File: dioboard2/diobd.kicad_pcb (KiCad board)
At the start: 2 copper layers, 58.4 x 15.2 mm, 9 parts, among them J1 Conn_01x03, J2 Conn_01x03, J3 Conn_01x03, J4 Conn_01x03

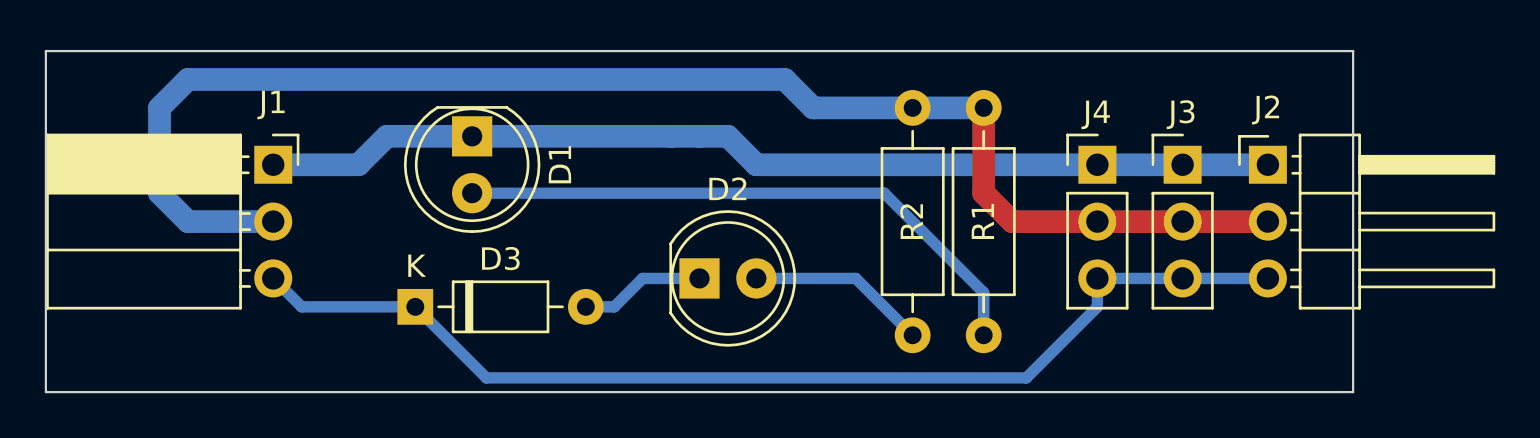
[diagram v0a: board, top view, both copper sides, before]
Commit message: delete traces and shrink board outline by moving parts
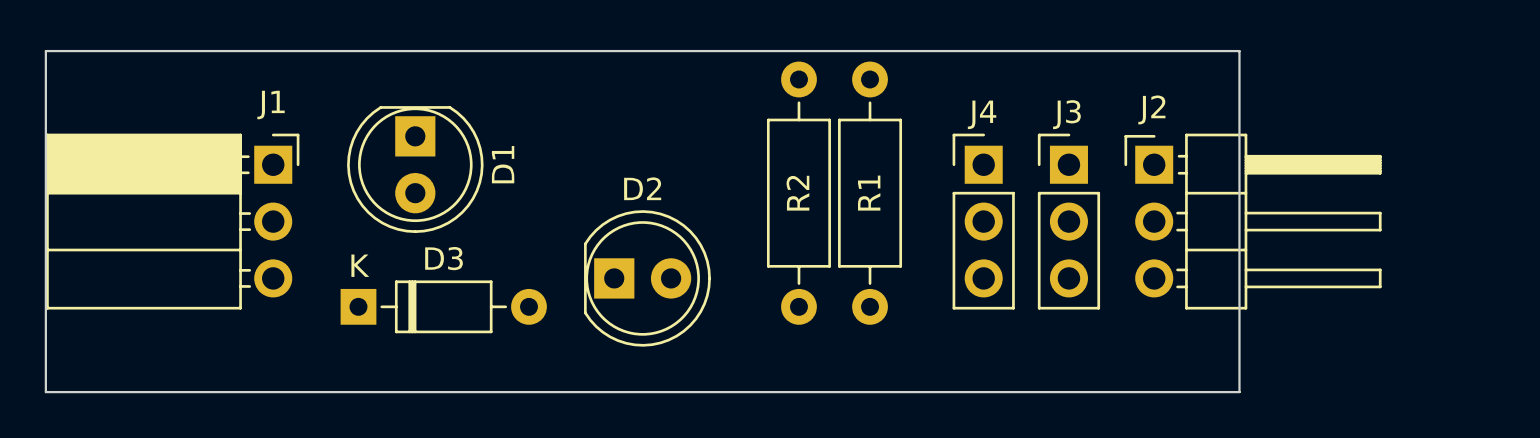
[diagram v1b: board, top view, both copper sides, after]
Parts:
- moved R2 5.24 mm to (127.6, 88.9)
- moved R1 5.24 mm to (130.8, 88.9)
- moved J2 5.08 mm to (143.5, 92.7)
- moved J3 5.08 mm to (139.7, 92.7)
- moved J4 5.08 mm to (135.9, 92.7)
- moved D2 3.81 mm to (119.4, 97.8)
- moved D1 2.54 mm to (110.5, 91.4)
- moved D3 2.54 mm to (108.0, 99.1)
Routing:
- net +5V: track 64.3 -> 0.00 mm
- net /signal: track 48.9 -> 0.00 mm
- net Earth: track 45.5 -> 0.00 mm
- net Net-(D1-Pad2): track 26.6 -> 0.00 mm
- net Net-(D2-Pad2): track 8.04 -> 0.00 mm
- net Net-(D2-Pad1): track 5.61 -> 0.00 mm
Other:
- board size 58.4 x 15.2 mm -> 53.3 x 15.2 mm
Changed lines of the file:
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@@
-(kicad_pcb (version 20171130) (host pcbnew 5.0.0)
+(kicad_pcb (version 20171130) (host pcbnew "(5.0.1)-3")
   (general
     (thickness 1.5748)
     (drawings 4)
-    (tracks 33)
+    (tracks 0)
     (zones 0)
     (modules 9)
@@
   )
   (setup
-    (last_trace_width 0.508)
+    (last_trace_width 0.2032)
     (user_trace_width 0.254)
     (user_trace_width 0.508)
@@
     (pad_drill 0.6)
     (pad_to_mask_clearance 0)
+    (solder_mask_min_width 0.25)
     (aux_axis_origin 0 0)
     (grid_origin 93.98 102.87)
-    (visible_elements FFFFFF7F)
+    (visible_elements 7FFFFFFF)
     (pcbplotparams
       (layerselection 0x010fc_ffffffff)
@@
   )
   (module LED_THT:LED_D5.0mm (layer F.Cu)
-    (at 113.03 91.44 270)
+    (at 110.49 91.44 270)
     (descr "LED, diameter 5.0mm, 2 pins, http://cdn-reichelt.de/documents/datenblatt/A500/LL-504BC2E-009.pdf")
     (tags "LED diameter 5.0mm 2 pins")
@@
   )
   (module LED_THT:LED_D5.0mm (layer F.Cu)
-    (at 123.19 97.79)
+    (at 119.38 97.79)
     (descr "LED, diameter 5.0mm, 2 pins, http://cdn-reichelt.de/documents/datenblatt/A500/LL-504BC2E-009.pdf")
     (tags "LED diameter 5.0mm 2 pins")
@@
   )
   (module Diode_THT:D_DO-35_SOD27_P7.62mm_Horizontal (layer F.Cu)
-    (at 110.49 99.06)
+    (at 107.95 99.06)
     (descr "Diode, DO-35_SOD27 series, Axial, Horizontal, pin pitch=7.62mm, , length*diameter=4*2mm^2, , http://www.diodes.com/_files/packages/DO-35.pdf")
     (tags "Diode DO-35_SOD27 series Axial Horizontal pin pitch 7.62mm  length 4mm diameter 2mm")
@@
   )
   (module Connector_PinHeader_2.54mm:PinHeader_1x03_P2.54mm_Horizontal (layer F.Cu)
-    (at 148.59 92.71)
+    (at 143.51 92.71)
     (descr "Through hole angled pin header, 1x03, 2.54mm pitch, 6mm pin length, single row")
     (tags "Through hole angled pin header THT 1x03 2.54mm single row")
@@
   )
   (module Connector_PinHeader_2.54mm:PinHeader_1x03_P2.54mm_Vertical (layer F.Cu)
-    (at 144.78 92.71)
+    (at 139.7 92.71)
     (descr "Through hole straight pin header, 1x03, 2.54mm pitch, single row")
     (tags "Through hole pin header THT 1x03 2.54mm single row")
@@
   )
   (module Connector_PinHeader_2.54mm:PinHeader_1x03_P2.54mm_Vertical (layer F.Cu)
-    (at 140.97 92.71)
+    (at 135.89 92.71)
     (descr "Through hole straight pin header, 1x03, 2.54mm pitch, single row")
     (tags "Through hole pin header THT 1x03 2.54mm single row")
@@
   )
   (module Resistor_THT:R_Axial_DIN0207_L6.3mm_D2.5mm_P10.16mm_Horizontal (layer F.Cu)
-    (at 135.89 90.17 270)
+    (at 130.81 88.9 270)
     (descr "Resistor, Axial_DIN0207 series, Axial, Horizontal, pin pitch=10.16mm, 0.25W = 1/4W, length*diameter=6.3*2.5mm^2, http://cdn-reichelt.de/documents/datenblatt/B400/1_4W%23YAG.pdf")
     (tags "Resistor Axial_DIN0207 series Axial Horizontal pin pitch 10.16mm 0.25W = 1/4W length 6.3mm diameter 2.5mm")
@@
   )
   (module Resistor_THT:R_Axial_DIN0207_L6.3mm_D2.5mm_P10.16mm_Horizontal (layer F.Cu)
-    (at 132.715 90.17 270)
+    (at 127.635 88.9 270)
     (descr "Resistor, Axial_DIN0207 series, Axial, Horizontal, pin pitch=10.16mm, 0.25W = 1/4W, length*diameter=6.3*2.5mm^2, http://cdn-reichelt.de/documents/datenblatt/B400/1_4W%23YAG.pdf")
     (tags "Resistor Axial_DIN0207 series Axial Horizontal pin pitch 10.16mm 0.25W = 1/4W length 6.3mm diameter 2.5mm")
@@
   )
   (gr_line (start 93.98 87.63) (end 93.98 102.87) (layer Edge.Cuts) (width 0.1))
-  (gr_line (start 152.4 87.63) (end 93.98 87.63) (layer Edge.Cuts) (width 0.1))
-  (gr_line (start 152.4 102.87) (end 152.4 87.63) (layer Edge.Cuts) (width 0.1))
-  (gr_line (start 93.98 102.87) (end 152.4 102.87) (layer Edge.Cuts) (width 0.1))
-  (segment (start 135.89 100.33) (end 135.89 98.425) (width 0.508) (layer B.Cu) (net 1))
-  (segment (start 131.445 93.98) (end 113.03 93.98) (width 0.508) (layer B.Cu) (net 1))
-  (segment (start 135.89 98.425) (end 131.445 93.98) (width 0.508) (layer B.Cu) (net 1))
-  (segment (start 104.14 92.71) (end 107.95 92.71) (width 1.016) (layer B.Cu) (net 2))
-  (segment (start 109.22 91.44) (end 113.03 91.44) (width 1.016) (layer B.Cu) (net 2))
-  (segment (start 107.95 92.71) (end 109.22 91.44) (width 1.016) (layer B.Cu) (net 2))
-  (segment (start 125.73 92.71) (end 148.59 92.71) (width 1.016) (layer B.Cu) (net 2))
-  (segment (start 113.03 91.44) (end 121.92 91.44) (width 1.016) (layer B.Cu) (net 2))
-  (segment (start 121.92 91.44) (end 123.19 91.44) (width 1.016) (layer B.Cu) (net 2))
-  (segment (start 123.19 91.44) (end 124.46 91.44) (width 1.016) (layer B.Cu) (net 2))
-  (segment (start 124.46 91.44) (end 125.73 92.71) (width 1.016) (layer B.Cu) (net 2))
-  (segment (start 118.11 99.06) (end 119.38 99.06) (width 0.508) (layer B.Cu) (net 3))
-  (segment (start 120.65 97.79) (end 123.19 97.79) (width 0.508) (layer B.Cu) (net 3))
-  (segment (start 119.38 99.06) (end 120.65 97.79) (width 0.508) (layer B.Cu) (net 3))
-  (segment (start 130.175 97.79) (end 132.715 100.33) (width 0.508) (layer B.Cu) (net 4))
-  (segment (start 125.73 97.79) (end 130.175 97.79) (width 0.508) (layer B.Cu) (net 4))
-  (segment (start 148.59 97.79) (end 140.97 97.79) (width 0.508) (layer B.Cu) (net 5))
-  (segment (start 113.665 102.235) (end 110.49 99.06) (width 0.508) (layer B.Cu) (net 5))
-  (segment (start 137.795 102.235) (end 113.665 102.235) (width 0.508) (layer B.Cu) (net 5))
-  (segment (start 140.97 99.06) (end 137.795 102.235) (width 0.508) (layer B.Cu) (net 5))
-  (segment (start 140.97 97.79) (end 140.97 99.06) (width 0.508) (layer B.Cu) (net 5))
-  (segment (start 105.41 99.06) (end 104.14 97.79) (width 0.508) (layer B.Cu) (net 5))
-  (segment (start 110.49 99.06) (end 105.41 99.06) (width 0.508) (layer B.Cu) (net 5))
-  (segment (start 128.27 90.17) (end 135.89 90.17) (width 1.016) (layer B.Cu) (net 6))
-  (segment (start 127 88.9) (end 128.27 90.17) (width 1.016) (layer B.Cu) (net 6))
-  (segment (start 100.33 88.9) (end 127 88.9) (width 1.016) (layer B.Cu) (net 6))
-  (segment (start 104.14 95.25) (end 100.33 95.25) (width 1.016) (layer B.Cu) (net 6))
-  (segment (start 99.06 93.98) (end 99.06 90.17) (width 1.016) (layer B.Cu) (net 6))
-  (segment (start 100.33 95.25) (end 99.06 93.98) (width 1.016) (layer B.Cu) (net 6))
-  (segment (start 99.06 90.17) (end 100.33 88.9) (width 1.016) (layer B.Cu) (net 6))
-  (segment (start 137.16 95.25) (end 135.89 93.98) (width 1.016) (layer F.Cu) (net 6))
-  (segment (start 135.89 93.98) (end 135.89 90.17) (width 1.016) (layer F.Cu) (net 6))
-  (segment (start 148.59 95.25) (end 137.16 95.25) (width 1.016) (layer F.Cu) (net 6))
+  (gr_line (start 147.32 87.63) (end 93.98 87.63) (layer Edge.Cuts) (width 0.1))
+  (gr_line (start 147.32 102.87) (end 147.32 87.63) (layer Edge.Cuts) (width 0.1))
+  (gr_line (start 93.98 102.87) (end 147.32 102.87) (layer Edge.Cuts) (width 0.1))
 )

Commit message: Finished preliminary routing
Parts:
- moved R1 1.27 mm to (130.8, 90.2)
- moved R2 1.27 mm to (127.6, 90.2)
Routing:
- net +5V: track 0.00 -> 45.8 mm
- net Net-(D1-Pad2): track 0.00 -> 44.8 mm
- net Earth: track 0.00 -> 44.0 mm
- net /signal: track 0.00 -> 42.5 mm
- net Net-(D2-Pad2): track 0.00 -> 6.77 mm
- net Net-(D2-Pad1): track 0.00 -> 4.34 mm
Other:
- net class Default: clearance 0.2032 -> 0.254; trace_width 0.2032 -> 0.254
- rule trace_clearance: 0.2032 -> 0.254
- rule trace_min: 0.2032 -> 0.254
- rule via_min_drill: 0.254 -> 0.381
- rule via_min_size: 0.635 -> 0.7874
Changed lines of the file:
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@@
     (thickness 1.5748)
     (drawings 4)
-    (tracks 0)
+    (tracks 40)
     (zones 0)
     (modules 9)
@@
   )
   (setup
-    (last_trace_width 0.2032)
+    (last_trace_width 0.254)
     (user_trace_width 0.254)
     (user_trace_width 0.508)
@@
     (user_trace_width 1.016)
     (user_trace_width 1.27)
-    (trace_clearance 0.2032)
+    (trace_clearance 0.254)
     (zone_clearance 0.508)
     (zone_45_only no)
-    (trace_min 0.2032)
+    (trace_min 0.254)
     (segment_width 0.2)
     (edge_width 0.1)
     (via_size 0.7874)
     (via_drill 0.381)
-    (via_min_size 0.635)
-    (via_min_drill 0.254)
+    (via_min_size 0.7874)
+    (via_min_drill 0.381)
     (uvia_size 0.7874)
     (uvia_drill 0.381)
@@
   (net 6 +5V)
   (net_class Default "This is the default net class."
-    (clearance 0.2032)
-    (trace_width 0.2032)
+    (clearance 0.254)
+    (trace_width 0.254)
     (via_dia 0.7874)
     (via_drill 0.381)
@@
     (uvia_drill 0.381)
     (diff_pair_gap 0.2032)
-    (diff_pair_width 0.2032)
+    (diff_pair_width 0.254)
     (add_net +5V)
     (add_net /signal)
@@
   )
   (module Resistor_THT:R_Axial_DIN0207_L6.3mm_D2.5mm_P10.16mm_Horizontal (layer F.Cu)
-    (at 130.81 88.9 270)
+    (at 130.81 90.17 270)
     (descr "Resistor, Axial_DIN0207 series, Axial, Horizontal, pin pitch=10.16mm, 0.25W = 1/4W, length*diameter=6.3*2.5mm^2, http://cdn-reichelt.de/documents/datenblatt/B400/1_4W%23YAG.pdf")
     (tags "Resistor Axial_DIN0207 series Axial Horizontal pin pitch 10.16mm 0.25W = 1/4W length 6.3mm diameter 2.5mm")
@@
   )
   (module Resistor_THT:R_Axial_DIN0207_L6.3mm_D2.5mm_P10.16mm_Horizontal (layer F.Cu)
-    (at 127.635 88.9 270)
+    (at 127.635 90.17 270)
     (descr "Resistor, Axial_DIN0207 series, Axial, Horizontal, pin pitch=10.16mm, 0.25W = 1/4W, length*diameter=6.3*2.5mm^2, http://cdn-reichelt.de/documents/datenblatt/B400/1_4W%23YAG.pdf")
     (tags "Resistor Axial_DIN0207 series Axial Horizontal pin pitch 10.16mm 0.25W = 1/4W length 6.3mm diameter 2.5mm")
@@
   (gr_line (start 147.32 102.87) (end 147.32 87.63) (layer Edge.Cuts) (width 0.1))
   (gr_line (start 93.98 102.87) (end 147.32 102.87) (layer Edge.Cuts) (width 0.1))
+  (segment (start 102.87 93.98) (end 101.6 95.25) (width 0.254) (layer B.Cu) (net 1))
+  (segment (start 110.49 93.98) (end 102.87 93.98) (width 0.254) (layer B.Cu) (net 1))
+  (segment (start 101.6 95.25) (end 101.6 99.06) (width 0.254) (layer B.Cu) (net 1))
+  (segment (start 130.010001 101.129999) (end 130.81 100.33) (width 0.254) (layer B.Cu) (net 1))
+  (segment (start 101.6 99.06) (end 105.02979 102.48979) (width 0.254) (layer B.Cu) (net 1))
+  (segment (start 105.02979 102.48979) (end 128.65021 102.48979) (width 0.254) (layer B.Cu) (net 1))
+  (segment (start 128.65021 102.48979) (end 130.010001 101.129999) (width 0.254) (layer B.Cu) (net 1))
+  (segment (start 143.51 92.71) (end 135.89 92.71) (width 1.016) (layer B.Cu) (net 2))
+  (segment (start 112.406 91.44) (end 110.49 91.44) (width 1.016) (layer B.Cu) (net 2))
+  (segment (start 115.45479 88.39121) (end 112.406 91.44) (width 1.016) (layer B.Cu) (net 2))
+  (segment (start 133.43721 88.39121) (end 115.45479 88.39121) (width 1.016) (layer B.Cu) (net 2))
+  (segment (start 135.89 90.844) (end 133.43721 88.39121) (width 1.016) (layer B.Cu) (net 2))
+  (segment (start 135.89 92.71) (end 135.89 90.844) (width 1.016) (layer B.Cu) (net 2))
+  (segment (start 104.14 92.71) (end 106.68 92.71) (width 1.016) (layer B.Cu) (net 2))
+  (segment (start 107.95 91.44) (end 110.49 91.44) (width 1.016) (layer B.Cu) (net 2))
+  (segment (start 106.68 92.71) (end 107.95 91.44) (width 1.016) (layer B.Cu) (net 2))
+  (segment (start 115.57 99.06) (end 118.11 99.06) (width 0.254) (layer B.Cu) (net 3))
+  (segment (start 118.11 99.06) (end 119.38 97.79) (width 0.254) (layer B.Cu) (net 3))
+  (segment (start 121.92 97.79) (end 124.46 100.33) (width 0.254) (layer B.Cu) (net 4))
+  (segment (start 124.46 100.33) (end 127.635 100.33) (width 0.254) (layer B.Cu) (net 4))
+  (segment (start 135.89 97.79) (end 143.51 97.79) (width 0.254) (layer B.Cu) (net 5))
+  (segment (start 125.741592 97.79) (end 123.201592 95.25) (width 0.254) (layer B.Cu) (net 5))
+  (segment (start 135.89 97.79) (end 125.741592 97.79) (width 0.254) (layer B.Cu) (net 5))
+  (segment (start 109.004 99.06) (end 110.274 97.79) (width 0.254) (layer B.Cu) (net 5))
+  (segment (start 107.95 99.06) (end 109.004 99.06) (width 0.254) (layer B.Cu) (net 5))
+  (segment (start 110.274 97.79) (end 115.57 97.79) (width 0.254) (layer B.Cu) (net 5))
+  (segment (start 115.57 97.79) (end 118.11 95.25) (width 0.254) (layer B.Cu) (net 5))
+  (segment (start 118.11 95.25) (end 123.201592 95.25) (width 0.254) (layer B.Cu) (net 5))
+  (segment (start 104.14 97.79) (end 105.41 99.06) (width 0.254) (layer B.Cu) (net 5))
+  (segment (start 105.41 99.06) (end 107.95 99.06) (width 0.254) (layer B.Cu) (net 5))
+  (segment (start 143.51 95.25) (end 135.89 95.25) (width 1.016) (layer B.Cu) (net 6))
+  (segment (start 135.89 95.25) (end 133.35 95.25) (width 1.016) (layer B.Cu) (net 6))
+  (segment (start 133.35 95.25) (end 130.81 92.71) (width 1.016) (layer B.Cu) (net 6))
+  (segment (start 130.81 92.71) (end 130.81 90.17) (width 1.016) (layer B.Cu) (net 6))
+  (segment (start 130.81 90.17) (end 127.635 90.17) (width 1.016) (layer B.Cu) (net 6))
+  (segment (start 127.635 90.17) (end 123.825 93.98) (width 1.016) (layer B.Cu) (net 6))
+  (segment (start 123.825 93.98) (end 116.84 93.98) (width 1.016) (layer B.Cu) (net 6))
+  (segment (start 104.989999 96.099999) (end 104.14 95.25) (width 1.016) (layer B.Cu) (net 6))
+  (segment (start 114.720001 96.099999) (end 104.989999 96.099999) (width 1.016) (layer B.Cu) (net 6))
+  (segment (start 116.84 93.98) (end 114.720001 96.099999) (width 1.016) (layer B.Cu) (net 6))
 )

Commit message: added silkscreen
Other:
- board text added: "4795 EASTBOTS DIO TESTER"
- board text added: "POWER"
- board text added: "SIGNAL"
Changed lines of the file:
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@@
-(kicad_pcb (version 20171130) (host pcbnew "(5.0.1)-3")
+(kicad_pcb (version 20171130) (host pcbnew 5.0.1-33cea8e~68~ubuntu16.04.1)
   (general
     (thickness 1.5748)
-    (drawings 4)
+    (drawings 9)
     (tracks 40)
     (zones 0)
@@
   (layers
     (0 F.Cu signal)
-    (31 B.Cu signal)
+    (31 B.Cu signal hide)
     (32 B.Adhes user)
     (33 F.Adhes user)
@@
     (descr "LED, diameter 5.0mm, 2 pins, http://cdn-reichelt.de/documents/datenblatt/A500/LL-504BC2E-009.pdf")
     (tags "LED diameter 5.0mm 2 pins")
-    (fp_text reference D2 (at 1.27 -3.96) (layer F.SilkS)
+    (fp_text reference D2 (at 5.08 3.81) (layer F.SilkS)
       (effects (font (size 1 1) (thickness 0.15)))
     )
@@
     )
   )
+  (gr_text "4795 EASTBOTS DIO TESTER" (at 110.49 88.9) (layer B.SilkS)
+    (effects (font (size 1.5 1.5) (thickness 0.3)) (justify mirror))
+  )
+  (gr_line (start 123.19 92.71) (end 124.46 92.71) (layer F.SilkS) (width 0.2))
+  (gr_line (start 116.84 92.71) (end 123.19 92.71) (layer F.SilkS) (width 0.2))
+  (gr_text SIGNAL (at 120.65 93.98) (layer F.SilkS)
+    (effects (font (size 1.5 1.5) (thickness 0.3)))
+  )
+  (gr_text POWER (at 110.49 88.9) (layer F.SilkS)
+    (effects (font (size 1.5 1.5) (thickness 0.3)))
+  )
   (gr_line (start 93.98 87.63) (end 93.98 102.87) (layer Edge.Cuts) (width 0.1))

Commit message: move some labels on the assembly-drawing layer, add lines on fab layer pointing to parts from labels that are outside the board outline.
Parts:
- J1: value Conn_01x03 -> socket_1x3
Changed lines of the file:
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@@
   (general
     (thickness 1.5748)
-    (drawings 9)
+    (drawings 11)
     (tracks 40)
     (zones 0)
@@
     (visible_elements 7FFFFFFF)
     (pcbplotparams
-      (layerselection 0x010fc_ffffffff)
+      (layerselection 0x010f0_ffffffff)
       (usegerberextensions false)
       (usegerberattributes false)
@@
       (outputformat 1)
       (mirror false)
-      (drillshape 1)
+      (drillshape 0)
       (scaleselection 1)
-      (outputdirectory ""))
+      (outputdirectory "gbr"))
   )
   (net 0 "")
@@
       (effects (font (size 1 1) (thickness 0.15)))
     )
-    (fp_text value YELLOW_5mm (at 1.27 3.96 270) (layer F.Fab)
+    (fp_text value YELLOW_5mm (at -5.08 0) (layer F.Fab)
       (effects (font (size 1 1) (thickness 0.15)))
     )
@@
       (effects (font (size 1 1) (thickness 0.15)))
     )
-    (fp_text value RED_5mm (at 1.27 3.96) (layer F.Fab)
+    (fp_text value RED_5mm (at 0 7.62) (layer F.Fab)
       (effects (font (size 1 1) (thickness 0.15)))
     )
@@
       (effects (font (size 1 1) (thickness 0.15)))
     )
-    (fp_text value Conn_01x03 (at -4.38 7.85) (layer F.Fab)
+    (fp_text value socket_1x3 (at -2.54 12.7) (layer F.Fab)
       (effects (font (size 1 1) (thickness 0.15)))
     )
@@
       (effects (font (size 1 1) (thickness 0.15)))
     )
-    (fp_text value Conn_01x03 (at 4.385 7.35) (layer F.Fab)
+    (fp_text value Conn_01x03 (at 4.385 8.89) (layer F.Fab)
       (effects (font (size 1 1) (thickness 0.15)))
     )
@@
       (effects (font (size 1 1) (thickness 0.15)))
     )
-    (fp_text value Conn_01x03 (at 0 7.41) (layer F.Fab)
+    (fp_text value Conn_01x03 (at 2.54 11.43) (layer F.Fab)
       (effects (font (size 1 1) (thickness 0.15)))
     )
@@
       (effects (font (size 1 1) (thickness 0.15)))
     )
-    (fp_text value Conn_01x03 (at 0 7.41) (layer F.Fab)
+    (fp_text value Conn_01x03 (at 0 12.7) (layer F.Fab)
       (effects (font (size 1 1) (thickness 0.15)))
     )
@@
     )
   )
+  (gr_line (start 119.38 104.14) (end 120.65 101.6) (layer F.Fab) (width 0.2))
+  (gr_line (start 102.87 105.41) (end 101.6 100.33) (layer F.Fab) (width 0.2))
   (gr_text "4795 EASTBOTS DIO TESTER" (at 110.49 88.9) (layer B.SilkS)
     (effects (font (size 1.5 1.5) (thickness 0.3)) (justify mirror))
